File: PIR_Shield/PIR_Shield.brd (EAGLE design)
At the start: 77.6 x 37 mm, 13 parts

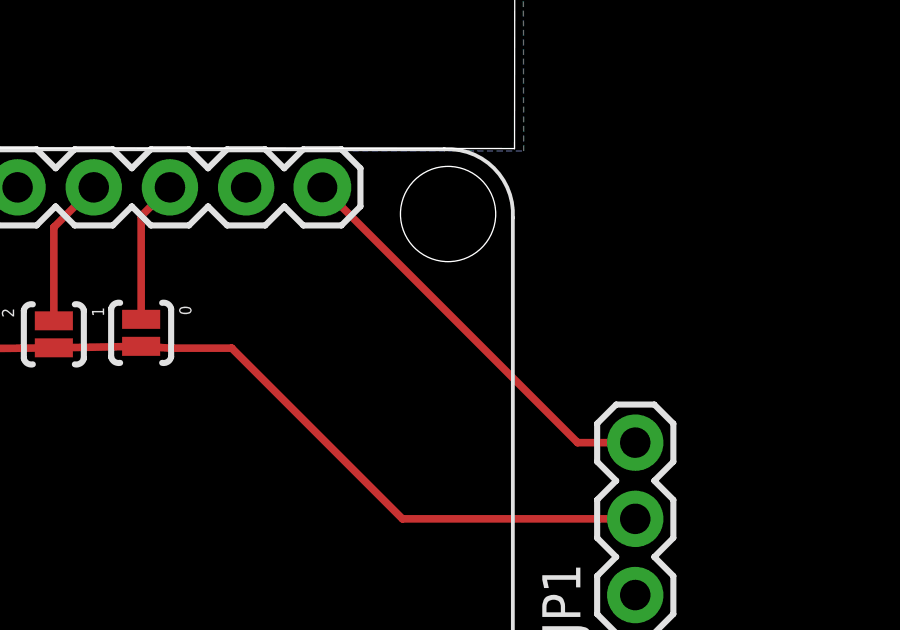
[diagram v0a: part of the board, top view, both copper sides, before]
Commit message: Updated the i2c pins to all shields to use d11/d12  as these pins will have dual use with the upcoming wifimcu Added FM24W256  Fram shield Added X95840 Digital potentiometer Shield Added AD5696 DAC Shield
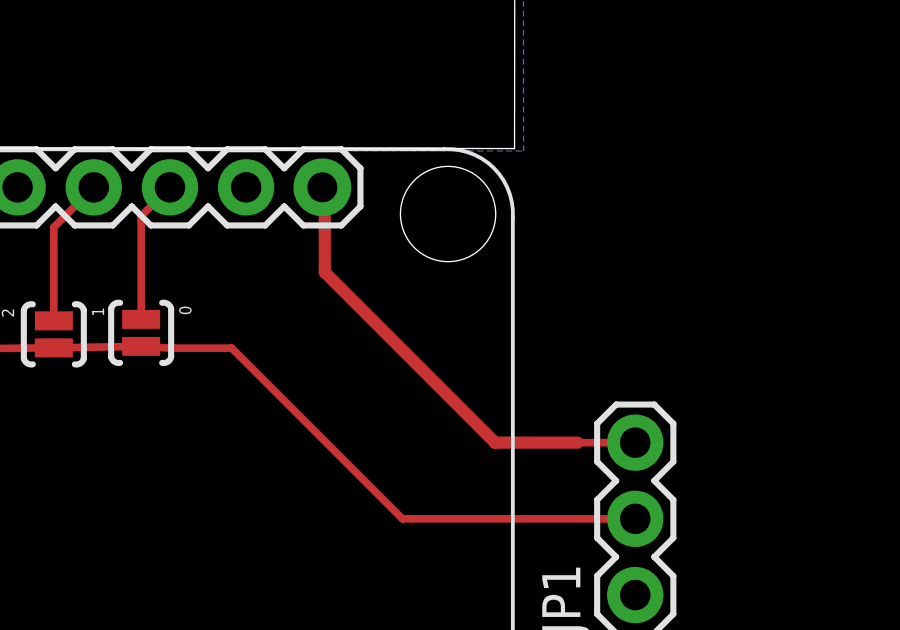
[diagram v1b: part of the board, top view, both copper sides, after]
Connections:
- net GND: no longer U$1.24
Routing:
- net 3.3V: track 14.0 -> 15.6 mm
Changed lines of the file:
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@@
 <contactref element="U$1" pad="14"/>
 <contactref element="U$1" pad="10"/>
-<contactref element="U$1" pad="24"/>
 <contactref element="U$1" pad="17"/>
 <polygon width="0.4064" layer="16">
@@
 <contactref element="JP1" pad="3"/>
 <wire x1="52.79" y1="21.49" x2="50.87" y2="21.49" width="0.254" layer="1"/>
-<wire x1="50.87" y1="21.49" x2="42.36" y2="30" width="0.254" layer="1"/>
+<wire x1="50.87" y1="21.49" x2="48.12" y2="21.49" width="0.4064" layer="1"/>
+<wire x1="48.12" y1="21.49" x2="42.44" y2="27.17" width="0.4064" layer="1"/>
+<wire x1="42.44" y1="27.17" x2="42.44" y2="29.92" width="0.4064" layer="1"/>
+<wire x1="42.44" y1="29.92" x2="42.36" y2="30" width="0.4064" layer="1"/>
 </signal>
 <signal name="N$2">
